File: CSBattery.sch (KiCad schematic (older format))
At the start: 1 part

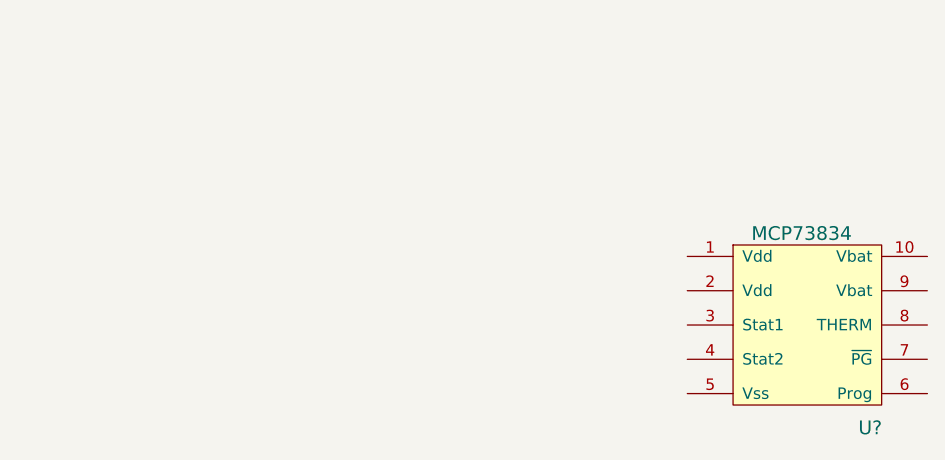
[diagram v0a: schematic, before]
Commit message: updated schematic with USB and added a gitignore file
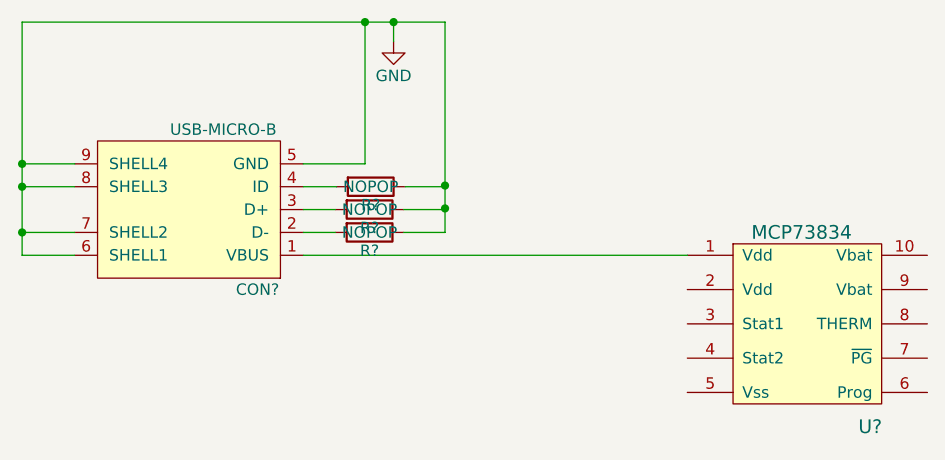
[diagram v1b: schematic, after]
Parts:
- added CON?: USB-MICRO-B, symbol USB-MICRO-B
- added R? (x3): NOPOP, symbol R
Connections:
- net at U?.1 (Vdd): now also CON?.1 (VBUS)
- new net: CON?.2 (D-), R?.2
- new net: CON?.3 (D+), R?.2
- new net: CON?.4 (ID), R?.2
- new net GND: CON?.5 (GND), CON?.6 (SHELL1), CON?.7 (SHELL2), CON?.8 (SHELL3), CON?.9 (SHELL4), R?.1, R?.1, R?.1
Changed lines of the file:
@@
 L MCP73834 U?
 U 1 1 55376E6C
-P 5400 2800
-F 0 "U?" H 5650 2300 60  0000 C CNN
-F 1 "MCP73834" H 5350 3150 60  0000 C CNN
-F 2 "" H 5500 2800 60  0000 C CNN
-F 3 "" H 5500 2800 60  0000 C CNN
-	1    5400 2800
+P 5400 2795
+F 0 "U?" H 5650 2295 60  0000 C CNN
+F 1 "MCP73834" H 5350 3145 60  0000 C CNN
+F 2 "" H 5500 2795 60  0000 C CNN
+F 3 "" H 5500 2795 60  0000 C CNN
+	1    5400 2795
 	1    0    0    -1
 $EndComp
+$Comp
+L USB-MICRO-B CON?
+U 1 1 5537FC70
+P 2670 2345
+F 0 "CON?" H 2370 2695 50  0000 C CNN
+F 1 "USB-MICRO-B" H 2520 1995 50  0000 C CNN
+F 2 "" H 2670 2245 50  0000 C CNN
+F 3 "" H 2670 2245 50  0000 C CNN
+	1    2670 2345
+	-1   0    0    1
+$EndComp
+$Comp
+L GND #PWR?
+U 1 1 5537FE4F
+P 3565 1610
+F 0 "#PWR?" H 3565 1360 50  0001 C CNN
+F 1 "GND" H 3565 1460 50  0000 C CNN
+F 2 "" H 3565 1610 60  0000 C CNN
+F 3 "" H 3565 1610 60  0000 C CNN
+	1    3565 1610
+	1    0    0    -1
+$EndComp
+Wire Wire Line
+	1940 2545 2170 2545
+Wire Wire Line
+	1940 1525 1940 2545
+Wire Wire Line
+	1940 1525 3790 1525
+Wire Wire Line
+	3565 1525 3565 1610
+Wire Wire Line
+	3170 2145 3440 2145
+Wire Wire Line
+	3440 2145 3440 1525
+Connection ~ 3440 1525
+Wire Wire Line
+	2170 2145 1940 2145
+Connection ~ 1940 2145
+Wire Wire Line
+	2170 2245 1940 2245
+Connection ~ 1940 2245
+Wire Wire Line
+	2170 2445 1940 2445
+Connection ~ 1940 2445
+Wire Wire Line
+	3170 2545 4850 2545
+$Comp
+L R R?
+U 1 1 5537FFD0
+P 3465 2245
+F 0 "R?" V 3545 2245 50  0000 C CNN
+F 1 "NOPOP" V 3465 2245 50  0000 C CNN
+F 2 "" V 3395 2245 30  0000 C CNN
+F 3 "" H 3465 2245 30  0000 C CNN
+	1    3465 2245
+	0    1    1    0
+$EndComp
+$Comp
+L R R?
+U 1 1 55380031
+P 3460 2345
+F 0 "R?" V 3540 2345 50  0000 C CNN
+F 1 "NOPOP" V 3460 2345 50  0000 C CNN
+F 2 "" V 3390 2345 30  0000 C CNN
+F 3 "" H 3460 2345 30  0000 C CNN
+	1    3460 2345
+	0    1    1    0
+$EndComp
+$Comp
+L R R?
+U 1 1 5538005A
+P 3460 2445
+F 0 "R?" V 3540 2445 50  0000 C CNN
+F 1 "NOPOP" V 3460 2445 50  0000 C CNN
+F 2 "" V 3390 2445 30  0000 C CNN
+F 3 "" H 3460 2445 30  0000 C CNN
+	1    3460 2445
+	0    1    1    0
+$EndComp
+Wire Wire Line
+	3170 2245 3315 2245
+Wire Wire Line
+	3170 2345 3310 2345
+Wire Wire Line
+	3170 2445 3310 2445
+Wire Wire Line
+	3610 2445 3790 2445
+Wire Wire Line
+	3790 2445 3790 1525
+Connection ~ 3565 1525
+Wire Wire Line
+	3610 2345 3790 2345
+Wire Wire Line
+	3790 2345 3790 2340
+Connection ~ 3790 2340
+Wire Wire Line
+	3615 2245 3790 2245
+Wire Wire Line
+	3790 2245 3790 2240
+Connection ~ 3790 2240
 $EndSCHEMATC

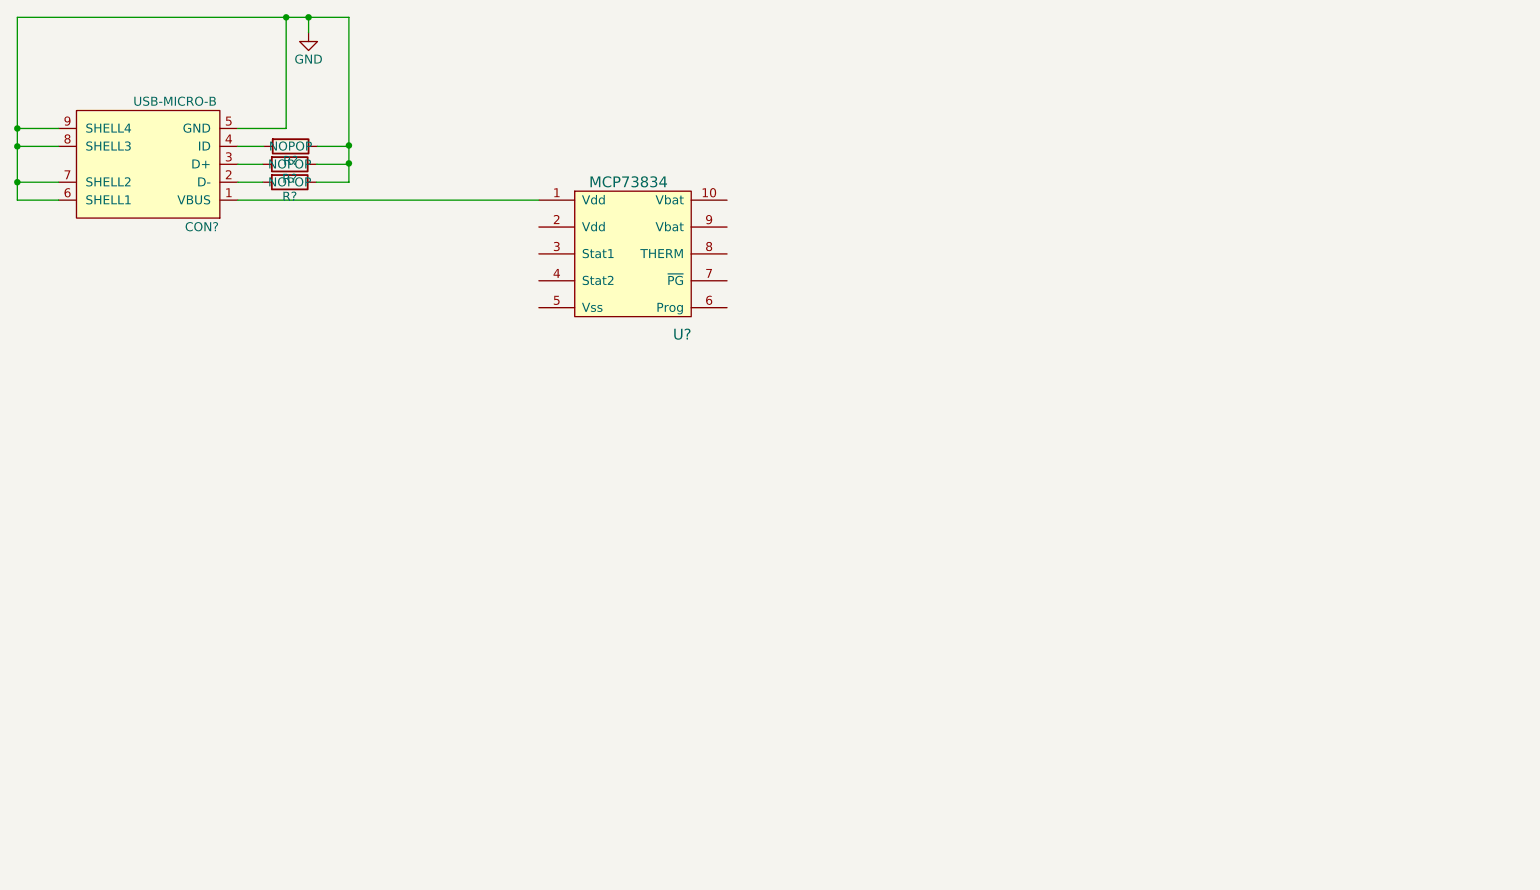
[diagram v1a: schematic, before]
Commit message: updated schematic with programmable voltage divider for charge current selection
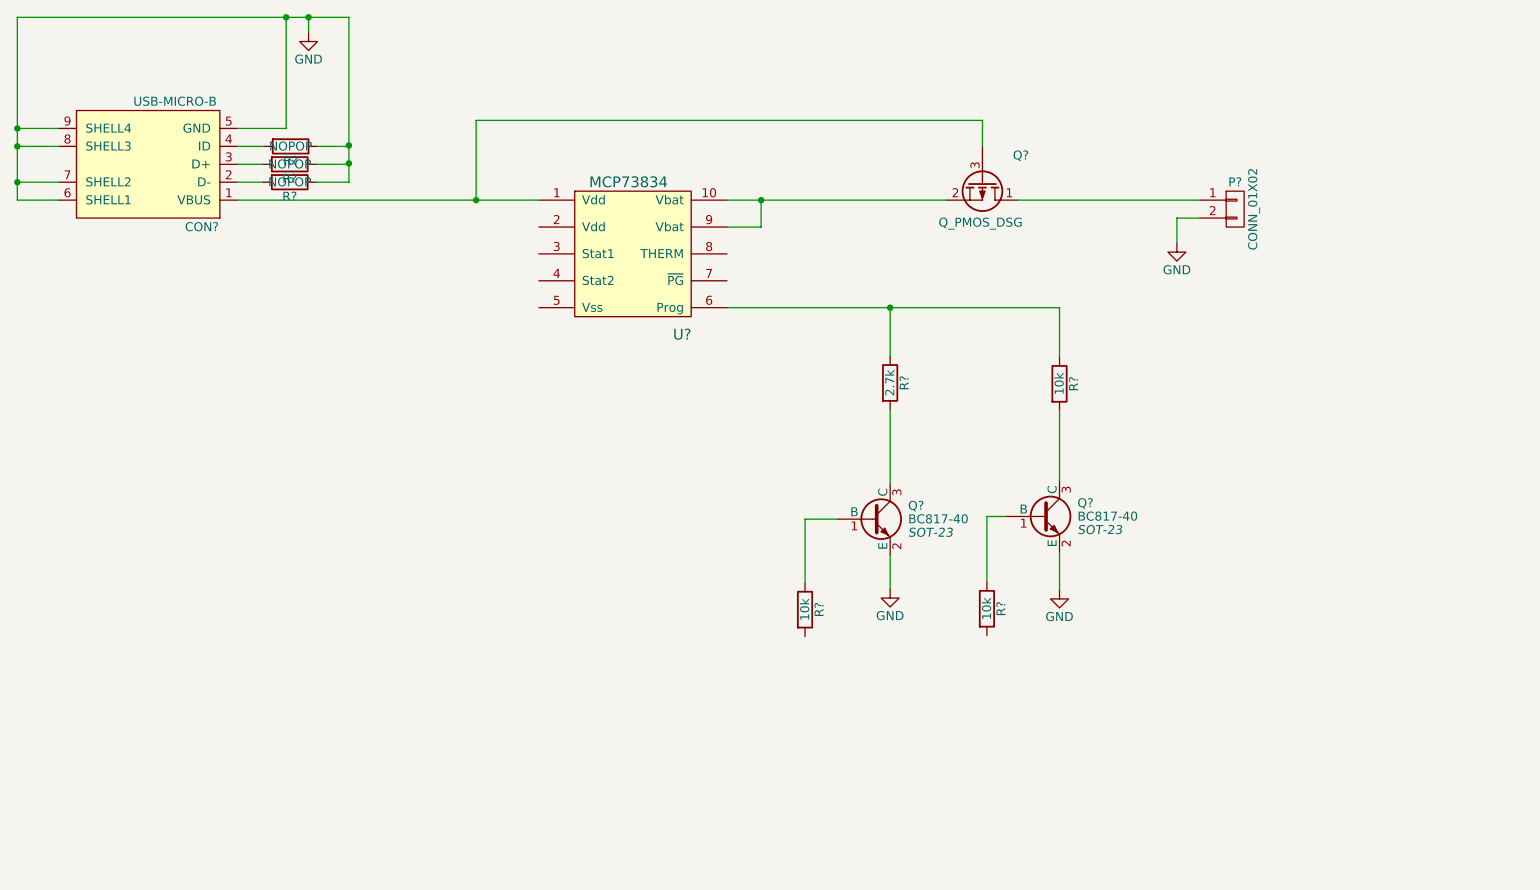
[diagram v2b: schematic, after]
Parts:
- added P?: CONN_01X02, symbol CONN_01X02
- added Q? (x2): BC817-40, SOT-23, symbol BC817-40
- added Q?: Q_PMOS_DSG, symbol Q_PMOS_DSG
- added R?: 2.7k, symbol R
- added R? (x3): 10k, symbol R
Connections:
- net GND: now also P?.2 (P2), Q?.2 (E), Q?.2 (E)
- net at CON?.1 (VBUS), U?.1 (Vdd): now also Q?.3 (G)
- net at U?.10 (Vbat): now also U?.9 (Vbat), Q?.2 (S)
- net at U?.6 (Prog): now also R?.1, R?.1
- new net: Q?.3 (C), R?.2 (x2)
- new net: Q?.1 (B), R?.1 (x2)
- new net: P?.1 (P1), Q?.1 (D)
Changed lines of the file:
@@
 	3170 2445 3310 2445
 Wire Wire Line
-	3610 2445 3790 2445
+	3790 2445 3610 2445
 Wire Wire Line
-	3790 2445 3790 1525
+	3790 1525 3790 2445
 Connection ~ 3565 1525
 Wire Wire Line
@@
 	3790 2245 3790 2240
 Connection ~ 3790 2240
+$Comp
+L R R?
+U 1 1 55381167
+P 6810 3565
+F 0 "R?" V 6890 3565 50  0000 C CNN
+F 1 "2.7k" V 6810 3565 50  0000 C CNN
+F 2 "" V 6740 3565 30  0000 C CNN
+F 3 "" H 6810 3565 30  0000 C CNN
+	1    6810 3565
+	1    0    0    -1
+$EndComp
+$Comp
+L R R?
+U 1 1 55381199
+P 7755 3570
+F 0 "R?" V 7835 3570 50  0000 C CNN
+F 1 "10k" V 7755 3570 50  0000 C CNN
+F 2 "" V 7685 3570 30  0000 C CNN
+F 3 "" H 7755 3570 30  0000 C CNN
+	1    7755 3570
+	1    0    0    -1
+$EndComp
+$Comp
+L BC817-40 Q?
+U 1 1 553811D2
+P 6710 4325
+F 0 "Q?" H 6910 4400 50  0000 L CNN
+F 1 "BC817-40" H 6910 4325 50  0000 L CNN
+F 2 "SOT-23" H 6910 4250 50  0000 L CIN
+F 3 "" H 6710 4325 50  0000 L CNN
+	1    6710 4325
+	1    0    0    -1
+$EndComp
+$Comp
+L BC817-40 Q?
+U 1 1 55381215
+P 7655 4310
+F 0 "Q?" H 7855 4385 50  0000 L CNN
+F 1 "BC817-40" H 7855 4310 50  0000 L CNN
+F 2 "SOT-23" H 7855 4235 50  0000 L CIN
+F 3 "" H 7655 4310 50  0000 L CNN
+	1    7655 4310
+	1    0    0    -1
+$EndComp
+$Comp
+L R R?
+U 1 1 5538125F
+P 6335 4830
+F 0 "R?" V 6415 4830 50  0000 C CNN
+F 1 "10k" V 6335 4830 50  0000 C CNN
+F 2 "" V 6265 4830 30  0000 C CNN
+F 3 "" H 6335 4830 30  0000 C CNN
+	1    6335 4830
+	1    0    0    -1
+$EndComp
+$Comp
+L R R?
+U 1 1 5538128A
+P 7350 4825
+F 0 "R?" V 7430 4825 50  0000 C CNN
+F 1 "10k" V 7350 4825 50  0000 C CNN
+F 2 "" V 7280 4825 30  0000 C CNN
+F 3 "" H 7350 4825 30  0000 C CNN
+	1    7350 4825
+	1    0    0    -1
+$EndComp
+Wire Wire Line
+	7350 4675 7350 4310
+Wire Wire Line
+	7350 4310 7455 4310
+Wire Wire Line
+	6335 4680 6335 4325
+Wire Wire Line
+	6335 4325 6510 4325
+$Comp
+L GND #PWR?
+U 1 1 55381534
+P 6810 4715
+F 0 "#PWR?" H 6810 4465 50  0001 C CNN
+F 1 "GND" H 6810 4565 50  0000 C CNN
+F 2 "" H 6810 4715 60  0000 C CNN
+F 3 "" H 6810 4715 60  0000 C CNN
+	1    6810 4715
+	1    0    0    -1
+$EndComp
+Wire Wire Line
+	6810 4715 6810 4525
+$Comp
+L GND #PWR?
+U 1 1 553815D6
+P 7755 4720
+F 0 "#PWR?" H 7755 4470 50  0001 C CNN
+F 1 "GND" H 7755 4570 50  0000 C CNN
+F 2 "" H 7755 4720 60  0000 C CNN
+F 3 "" H 7755 4720 60  0000 C CNN
+	1    7755 4720
+	1    0    0    -1
+$EndComp
+Wire Wire Line
+	7755 4720 7755 4510
+Wire Wire Line
+	7755 4110 7755 3720
+Wire Wire Line
+	6810 4125 6810 3715
+Wire Wire Line
+	5900 3145 7755 3145
+Wire Wire Line
+	7755 3145 7755 3420
+Wire Wire Line
+	6810 3415 6810 3145
+Connection ~ 6810 3145
+$Comp
+L Q_PMOS_DSG Q?
+U 1 1 55381C92
+P 7325 2445
+F 0 "Q?" V 7175 2705 50  0000 R CNN
+F 1 "Q_PMOS_DSG" V 7550 2670 50  0000 R CNN
+F 2 "" H 7525 2545 29  0000 C CNN
+F 3 "" H 7325 2445 60  0000 C CNN
+	1    7325 2445
+	0    1    1    0
+$EndComp
+Wire Wire Line
+	5900 2545 7125 2545
+Wire Wire Line
+	7325 2245 7325 2100
+Wire Wire Line
+	7325 2100 4500 2100
+Wire Wire Line
+	4500 2100 4500 2545
+Connection ~ 4500 2545
+$Comp
+L CONN_01X02 P?
+U 1 1 553820C5
+P 8735 2595
+F 0 "P?" H 8735 2745 50  0000 C CNN
+F 1 "CONN_01X02" V 8835 2595 50  0000 C CNN
+F 2 "" H 8735 2595 60  0000 C CNN
+F 3 "" H 8735 2595 60  0000 C CNN
+	1    8735 2595
+	1    0    0    -1
+$EndComp
+Wire Wire Line
+	7525 2545 8535 2545
+$Comp
+L GND #PWR?
+U 1 1 55382444
+P 8410 2785
+F 0 "#PWR?" H 8410 2535 50  0001 C CNN
+F 1 "GND" H 8410 2635 50  0000 C CNN
+F 2 "" H 8410 2785 60  0000 C CNN
+F 3 "" H 8410 2785 60  0000 C CNN
+	1    8410 2785
+	1    0    0    -1
+$EndComp
+Wire Wire Line
+	8410 2785 8410 2645
+Wire Wire Line
+	8410 2645 8535 2645
+Wire Wire Line
+	5900 2695 6090 2695
+Wire Wire Line
+	6090 2695 6090 2545
+Connection ~ 6090 2545
 $EndSCHEMATC

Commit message: updated schematic with power path and uController selectable charge range
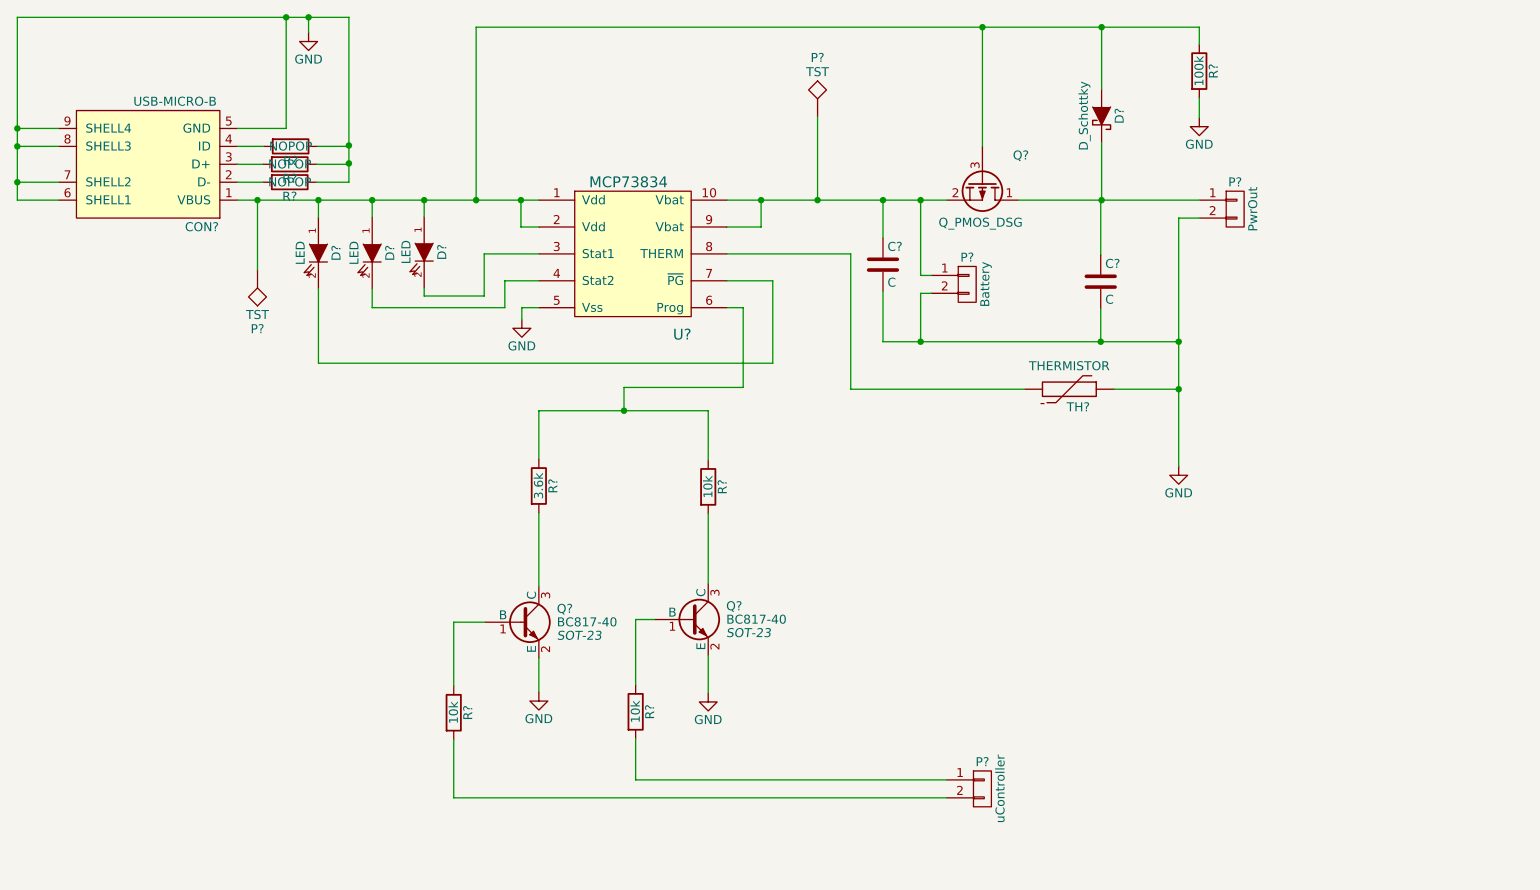
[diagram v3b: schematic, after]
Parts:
- added C? (x2): C, symbol C
- added D?: D_Schottky, symbol D_Schottky
- added D? (x3): LED, symbol LED
- added P?: Battery, symbol CONN_01X02
- added P? (x2): TST, symbol TST
- added P?: uController, symbol CONN_01X02
- added R?: 100k, symbol R
- added TH?: THERMISTOR, symbol THERMISTOR
- P?: value CONN_01X02 -> PwrOut
- R?: value 2.7k -> 3.6k
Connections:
- net GND: now also U?.5 (Vss), C?.2, C?.2, P?.2 (P2), R?.2, TH?.1
- net at CON?.1 (VBUS), Q?.3 (G), U?.1 (Vdd): now also U?.2 (Vdd), D?.1 (A), D?.1 (A), D?.1 (A), D?.1 (A), P?.1, R?.1
- net at Q?.2 (S), U?.10 (Vbat), U?.9 (Vbat): now also C?.1, P?.1, P?.1 (P1)
- net at U?.3 (Stat1): now also D?.2 (K)
- net at U?.4 (Stat2): now also D?.2 (K)
- net at U?.7 (~PG): now also D?.2 (K)
- net at U?.8 (THERM): now also TH?.2
- net at R?.2: now also P?.2 (P2)
- net at R?.2: now also P?.1 (P1)
- net at P?.1 (P1), Q?.1 (D): now also D?.2 (K)
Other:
- moved on the sheet: Q?, R?

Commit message: updated part numbers and changed Mosfet and Diode to an all in one package
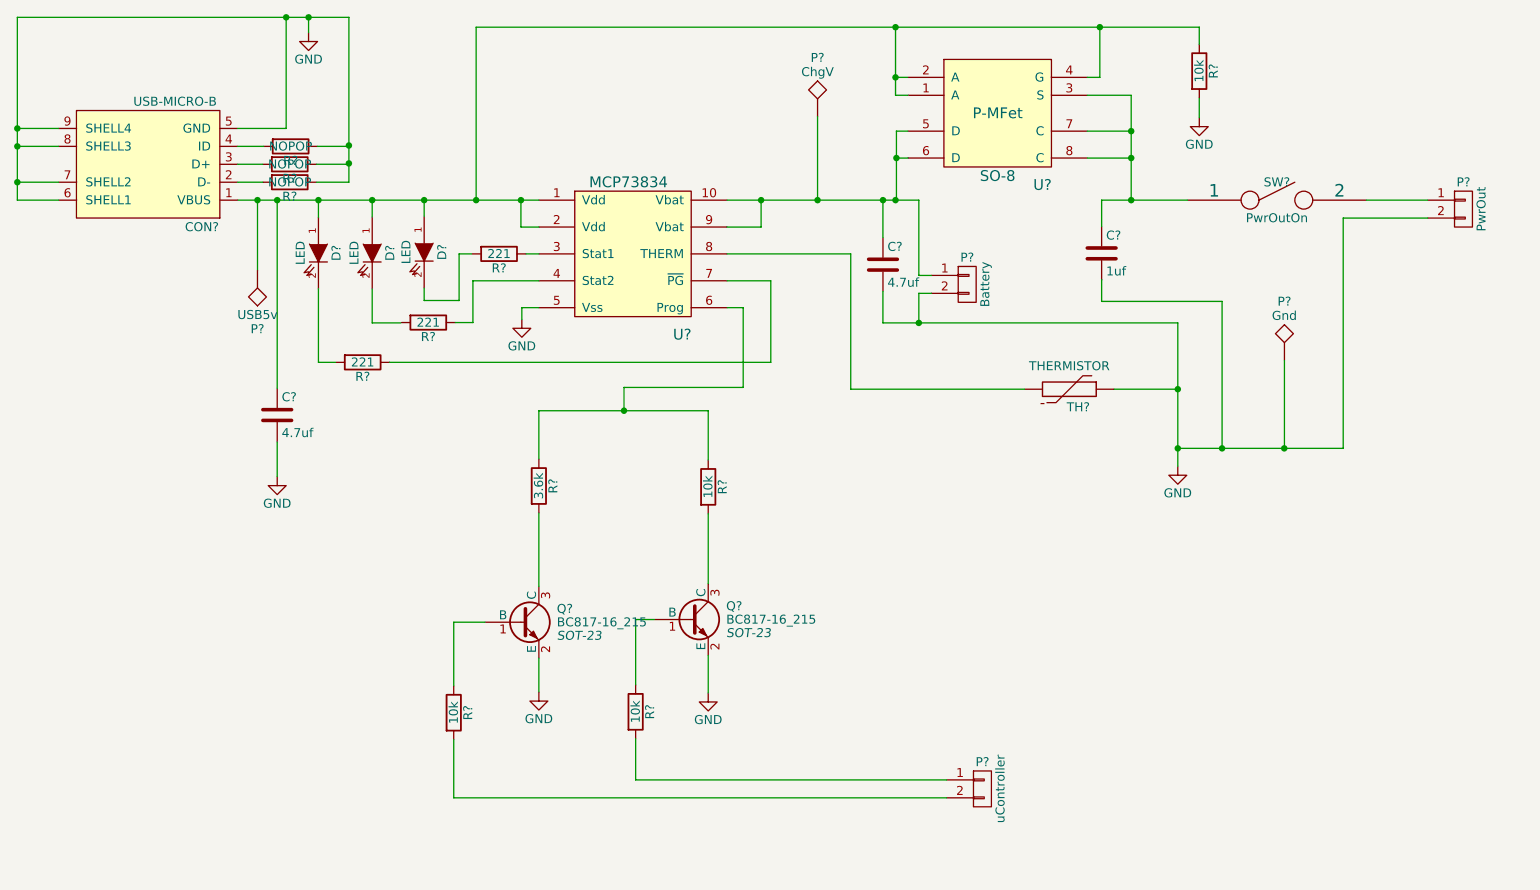
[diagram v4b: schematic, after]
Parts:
- removed D?: D_Schottky, symbol D_Schottky
- removed Q?: Q_PMOS_DSG, symbol Q_PMOS_DSG
- added C?: 4.7uf, symbol C
- added P?: Gnd, symbol TST
- added R? (x3): 221, symbol R
- added SW?: PwrOutOn, symbol SPST
- added U?: P-MFet, SO-8, symbol P-MFet
- C?: value C -> 1uf; MPN (none) -> Value
- C?: value C -> 4.7uf
- P?: value TST -> ChgV
- P?: value TST -> USB5v
- Q? (x2): value BC817-40 -> BC817-16_215; MPN (none) -> Value
- R?: value 100k -> 10k
- TH?: MPN (none) -> NTCLE100E3103JB0
- U?: MPN (none) -> MCP73834-FCI/UN
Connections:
- wire segments 85 -> 107
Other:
- moved on the sheet: C?, P?
